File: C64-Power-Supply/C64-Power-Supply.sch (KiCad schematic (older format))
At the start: 18 parts, among them J1 PWR_IN, J2 V_Select, J3 Conn_01x07, T1 Transformer_2P_2S

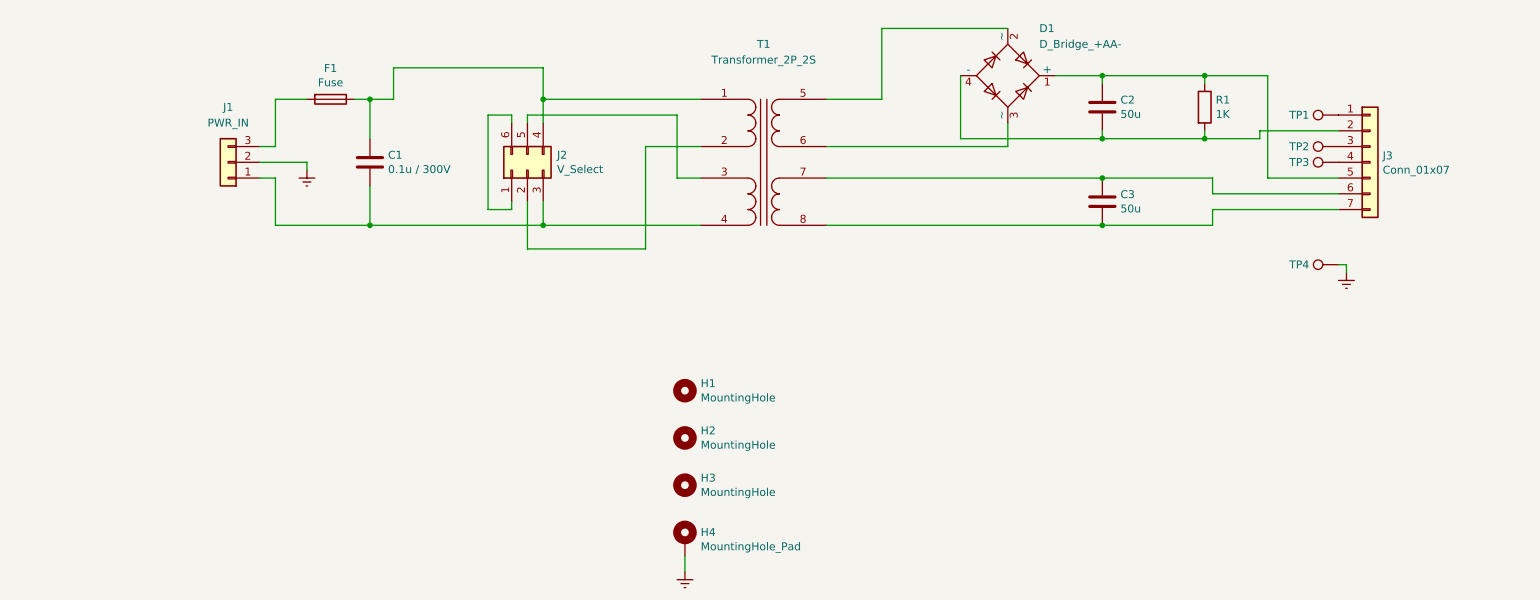
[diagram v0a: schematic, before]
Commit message: Added 5VDC regulation
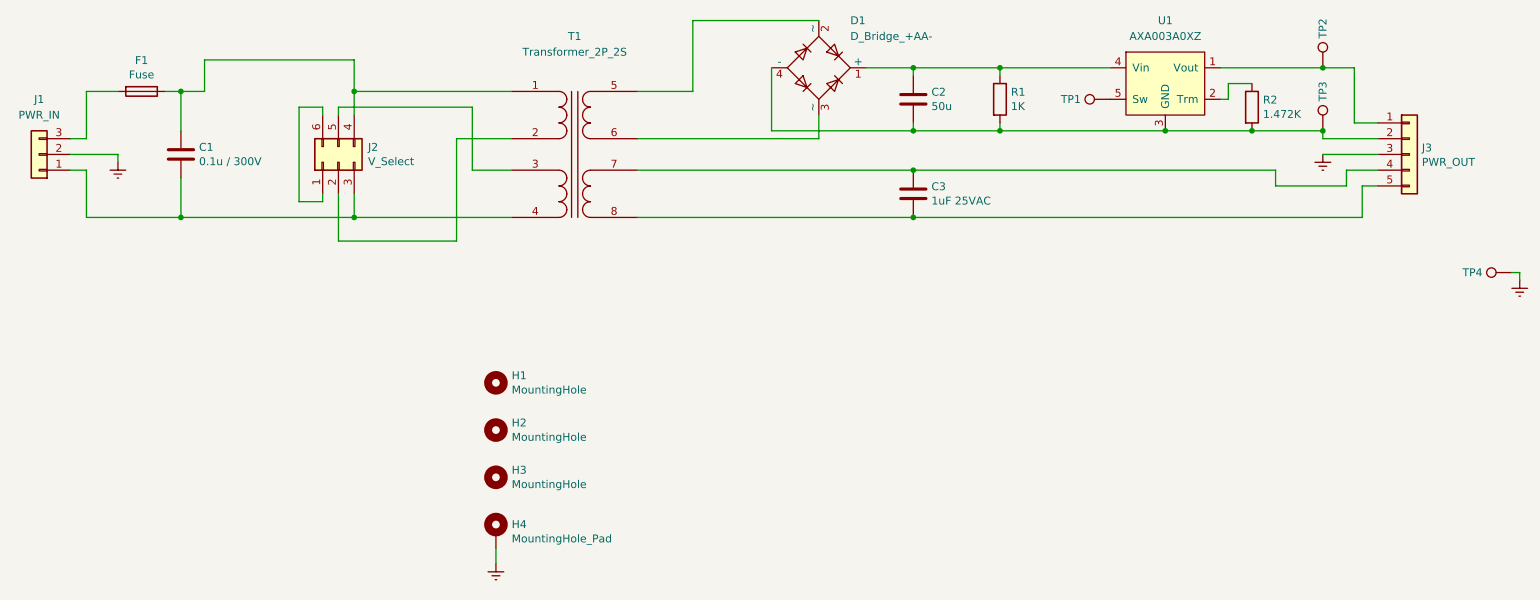
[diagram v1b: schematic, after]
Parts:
- removed J3: Conn_01x07, Connector_JST:JST_VH_B7P-VH_1x07_P3.96mm_Vertical, symbol Connector_Generic:Conn_01x07
- removed TP3: TestPoint, TestPoint:TestPoint_Pad_D2.5mm, symbol Connector:TestPoint
- added J3: PWR_OUT, Connector_JST:JST_VH_B5P-VH_1x05_P3.96mm_Vertical, symbol Connector_Generic:Conn_01x05
- added R2: 1.472K, Resistor_SMD:R_1206_3216Metric_Pad1.42x1.75mm_HandSolder, symbol Device:R
- added TP4: TestPoint, TestPoint:TestPoint_Pad_D2.5mm, symbol Connector:TestPoint
- added U1: AXA003A0XZ, MarkFromSales:AXA003A0XZ, symbol MFS_Power:AXA003A0XZ
- C3: value 50u -> 1uF 25VAC; footprint Capacitor_THT:CP_Axial_L25.0mm_D10.0mm_P30.00mm_Horizontal -> Capacitor_THT:C_Rect_L18.0mm_W11.0mm_P15.00mm_FKS3_FKP3
- renumbered TP4 to TP3
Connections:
- net Earth: now also J3.3 (Pin_3), TP4.1; no longer TP3.1
- net at C2.1, D1.1 (+), R1.1: now also U1.4 (Vin)
- net at C2.2, D1.4 (-), R1.2: now also TP3.1, J3.2 (Pin_2), R2.2, U1.3 (GND)
- net at C3.1, T1.7 (OUT2A): now also J3.4 (Pin_4)
- net at C3.2, T1.8 (OUT2B): now also J3.5 (Pin_5)
- net at TP1.1: now also U1.5 (Sw)
- net at TP2.1: now also J3.1 (Pin_1), U1.1 (Vout)
- new net: R2.1, U1.2 (Trm)
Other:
- moved on the sheet: C1, C2, C3, D1, F1, H1, H2, H3, H4, J1, J2, R1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
